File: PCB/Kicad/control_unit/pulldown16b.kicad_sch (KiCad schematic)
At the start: 16 parts

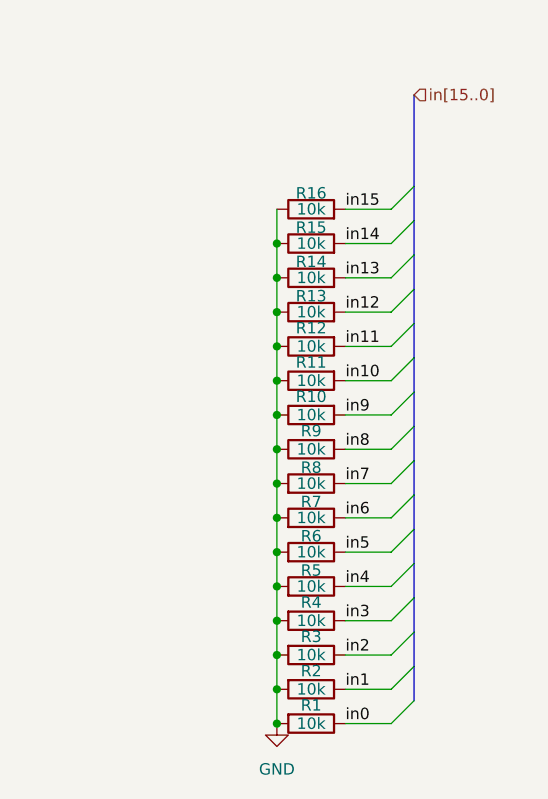
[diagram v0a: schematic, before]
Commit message: control unit schematic
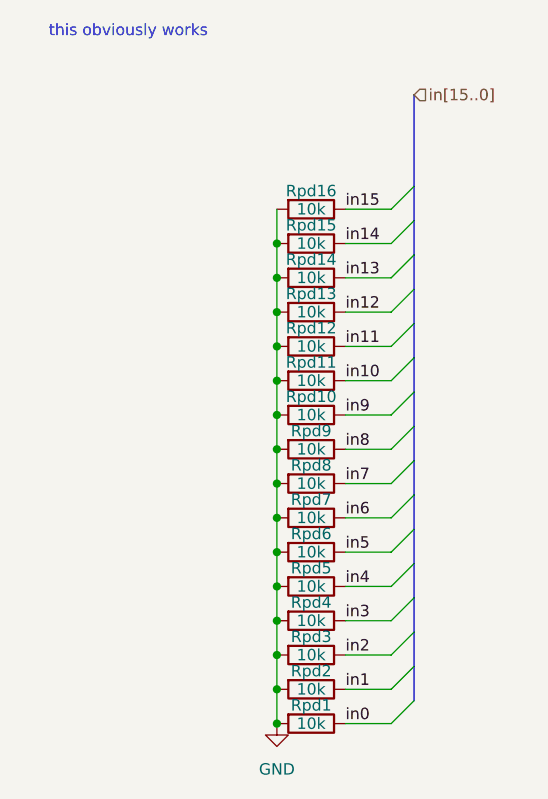
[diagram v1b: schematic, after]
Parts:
- removed R10, R11, R12, R13, R14, R15, R16, R2, R3, R4, R5, R6, R7, R8, R9: 10k, symbol Device:R
- added Rpd10, Rpd11, Rpd12, Rpd13, Rpd14, Rpd15, Rpd16, Rpd2, Rpd3, Rpd4, Rpd5, Rpd6, Rpd7, Rpd8, Rpd9: 10k, Resistor_SMD:R_0402_1005Metric, symbol Device:R
- Rpd1: renamed from R1; footprint (none) -> Resistor_SMD:R_0402_1005Metric
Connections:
- net GND: now also Rpd10.2, Rpd11.2, Rpd12.2, Rpd13.2, Rpd14.2, Rpd15.2, Rpd16.2, Rpd2.2, Rpd3.2, Rpd4.2, Rpd5.2, Rpd6.2, Rpd7.2, Rpd8.2, Rpd9.2
- net in1: now also Rpd2.1
- net in10: now also Rpd11.1
- net in11: now also Rpd12.1
- net in12: now also Rpd13.1
- net in13: now also Rpd14.1
- net in14: now also Rpd15.1
- net in15: now also Rpd16.1
- net in2: now also Rpd3.1
- net in3: now also Rpd4.1
- net in4: now also Rpd5.1
- net in5: now also Rpd6.1
- net in6: now also Rpd7.1
- net in7: now also Rpd8.1
- net in8: now also Rpd9.1
- net in9: now also Rpd10.1
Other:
- note added: "this obviously works"
- company: (none) -> AGH Logic Unit
- title: (none) -> 16 bit Pull Down
